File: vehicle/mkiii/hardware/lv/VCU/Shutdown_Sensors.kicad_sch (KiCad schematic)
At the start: 11 parts, among them Q5 SSM3K333R,LF, Q6 SSM3K333R,LF

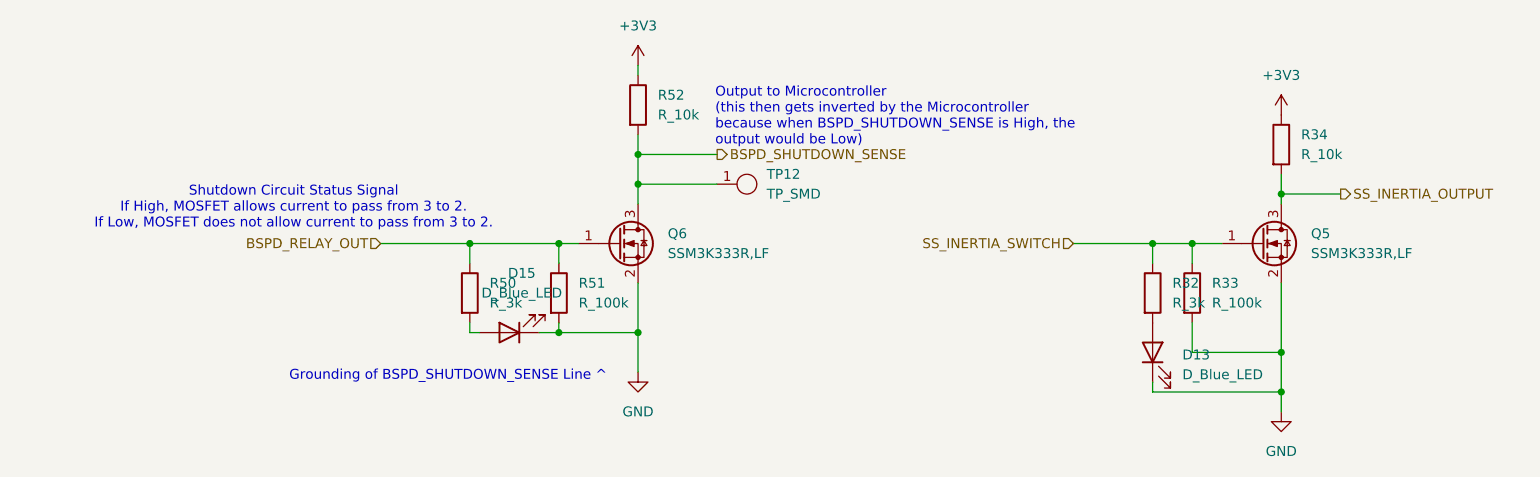
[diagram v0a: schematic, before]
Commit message: Layout completed, review required
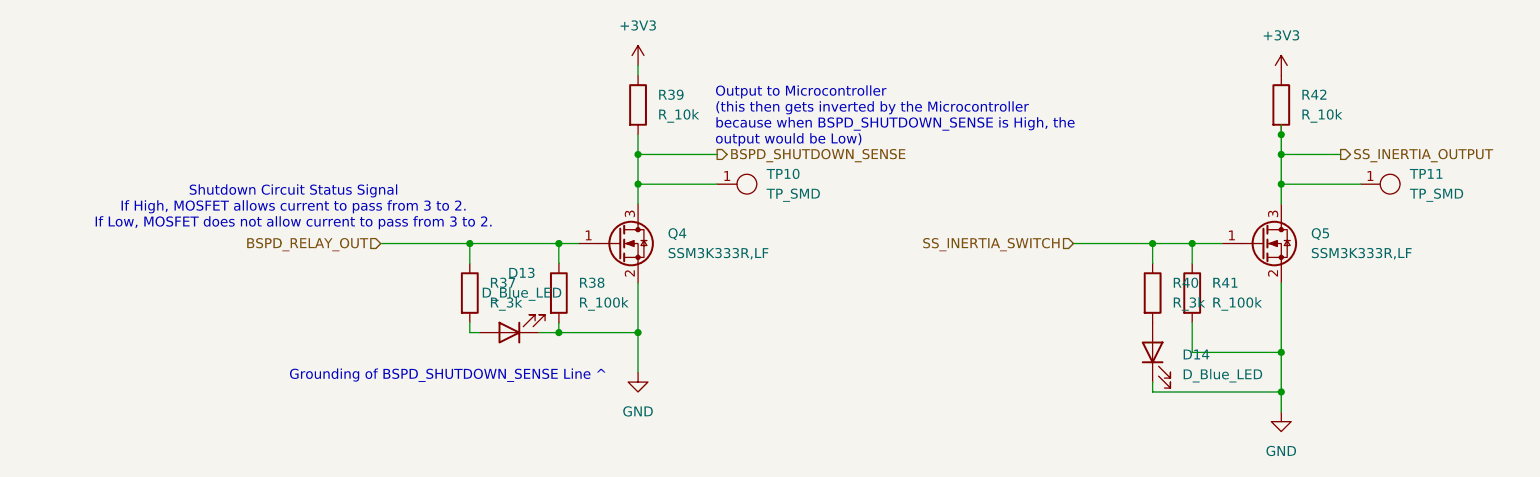
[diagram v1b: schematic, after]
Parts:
- added TP11: TP_SMD, OEM:TP_Hook_SMD, symbol OEM:TP_Hook_SMD
- renumbered D15 to D13, D13 to D14, Q6 to Q4, R50 to R37, R51 to R38, R52 to R39, R32 to R40, R33 to R41, R34 to R42, TP12 to TP10
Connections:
- net SS_INERTIA_OUTPUT: now also TP11.1
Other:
- moved on the sheet: R42
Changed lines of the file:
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@@
+	)
+	(junction
+		(at 201.93 83.82)
+		(diameter 0)
+		(color 0 0 0 0)
 	)
 	(junction
@@
 	)
 	(junction
+		(at 201.93 81.28)
+		(diameter 0)
+		(color 0 0 0 0)
+	)
+	(junction
 		(at 201.93 109.22)
 		(diameter 0)
@@
 	)
 	(junction
-		(at 201.93 88.9)
+		(at 201.93 87.63)
 		(diameter 0)
 		(color 0 0 0 0)
@@
 	(wire
 		(pts
+			(xy 201.93 87.63) (xy 201.93 90.17)
+		)
+		(stroke
+			(width 0)
+			(type default)
+		)
+	)
+	(wire
+		(pts
 			(xy 201.93 100.33) (xy 201.93 109.22)
 		)
@@
 	(wire
 		(pts
-			(xy 201.93 88.9) (xy 201.93 90.17)
-		)
-		(stroke
-			(width 0)
-			(type default)
-		)
-	)
-	(wire
-		(pts
 			(xy 86.36 95.25) (xy 97.79 95.25)
 		)
@@
 	(wire
 		(pts
-			(xy 201.93 86.36) (xy 201.93 88.9)
+			(xy 201.93 83.82) (xy 201.93 87.63)
+		)
+		(stroke
+			(width 0)
+			(type default)
+		)
+	)
+	(wire
+		(pts
+			(xy 201.93 81.28) (xy 201.93 83.82)
+		)
+		(stroke
+			(width 0)
+			(type default)
+		)
+	)
+	(wire
+		(pts
+			(xy 201.93 80.01) (xy 201.93 81.28)
 		)
 		(stroke
@@
 	(wire
 		(pts
-			(xy 201.93 88.9) (xy 209.55 88.9)
+			(xy 201.93 87.63) (xy 212.09 87.63)
+		)
+		(stroke
+			(width 0)
+			(type default)
+		)
+	)
+	(wire
+		(pts
+			(xy 201.93 83.82) (xy 209.55 83.82)
 		)
 		(stroke
@@
 	(hierarchical_label "SS_INERTIA_OUTPUT"
 		(shape output)
-		(at 209.55 88.9 0)
+		(at 209.55 83.82 0)
 		(effects
 			(font
@@
 	(symbol
 		(lib_id "OEM:R_10k_0.1W_0603")
-		(at 201.93 82.55 0)
+		(at 201.93 77.47 0)
 		(unit 1)
 		(exclude_from_sim no)
@@
 		(dnp no)
 		(fields_autoplaced yes)
-		(property "Reference" "R34"
-			(at 204.47 81.2799 0)
+		(property "Reference" "R42"
+			(at 204.47 76.1999 0)
 			(effects
 				(font
@@
 		)
 		(property "Value" "R_10k"
-			(at 204.47 83.8199 0)
+			(at 204.47 78.7399 0)
 			(effects
 				(font
@@
 		)
 		(property "Footprint" "OEM:R_0603_1608Metric"
-			(at 200.152 82.55 90)
+			(at 200.152 77.47 90)
 			(effects
 				(font
@@
 		)
 		(property "Datasheet" "https://www.mouser.com/datasheet/3/1099/1/SEI-RMCF_RMCP.pdf"
-			(at 201.93 82.55 0)
+			(at 201.93 77.47 0)
 			(effects
 				(font
@@
 		)
 		(property "Description" "RES 10K OHM 1% 1/10W 0603"
-			(at 201.93 82.55 0)
+			(at 201.93 77.47 0)
 			(effects
 				(font
@@
 		)
 		(property "MPN" "RMCF0603FT10K0"
-			(at 201.93 82.55 0)
+			(at 201.93 77.47 0)
 			(effects
 				(font
@@
 			(project "VCU"
 				(path "/ec5dd9e3-3092-4af4-bee1-94131d9ab7f8/f55c9820-8c9e-45b3-8461-692c1237659f"
-					(reference "R34")
+					(reference "R42")
 					(unit 1)
 				)
@@
 		(dnp no)
 		(fields_autoplaced yes)
-		(property "Reference" "R33"
+		(property "Reference" "R41"
 			(at 193.04 100.3299 0)
 			(effects
@@
 			(project "VCU"
 				(path "/ec5dd9e3-3092-4af4-bee1-94131d9ab7f8/f55c9820-8c9e-45b3-8461-692c1237659f"
-					(reference "R33")
+					(reference "R41")
+					(unit 1)
+				)
+			)
+		)
+	)
+	(symbol
+		(lib_id "OEM:TP_Hook_SMD")
+		(at 213.36 87.63 270)
+		(unit 1)
+		(exclude_from_sim no)
+		(in_bom yes)
+		(on_board yes)
+		(dnp no)
+		(fields_autoplaced yes)
+		(property "Reference" "TP11"
+			(at 218.44 86.3599 90)
+			(effects
+				(font
+					(size 1.27 1.27)
+				)
+				(justify left)
+			)
+		)
+		(property "Value" "TP_SMD"
+			(at 218.44 88.8999 90)
+			(effects
+				(font
+					(size 1.27 1.27)
+				)
+				(justify left)
+			)
+		)
+		(property "Footprint" "OEM:TP_Hook_SMD"
+			(at 209.55 87.63 0)
+			(effects
+				(font
+					(size 1.27 1.27)
+				)
+				(hide yes)
+			)
+		)
+		(property "Datasheet" "https://www.mouser.com/datasheet/3/201/1/5019.PDF"
+			(at 213.36 87.63 0)
+			(effects
+				(font
+					(size 1.27 1.27)
+				)
+				(hide yes)
+			)
+		)
+		(property "Description" "Test Point SMD Hook"
+			(at 213.36 87.63 0)
+			(effects
+				(font
+					(size 1.27 1.27)
+				)
+				(hide yes)
+			)
+		)
+		(property "MPN" "5019"
+			(at 213.36 87.63 0)
+			(effects
+				(font
+					(size 1.27 1.27)
+				)
+				(hide yes)
+			)
+		)
+		(pin "1"
+		)
+		(instances
+			(project "VCU"
+				(path "/ec5dd9e3-3092-4af4-bee1-94131d9ab7f8/f55c9820-8c9e-45b3-8461-692c1237659f"
+					(reference "TP11")
 					(unit 1)
 				)
@@
 		(dnp no)
 		(fields_autoplaced yes)
-		(property "Reference" "R52"
+		(property "Reference" "R39"
 			(at 121.92 76.1999 0)
 			(effects
@@
 			(project "VCU"
 				(path "/ec5dd9e3-3092-4af4-bee1-94131d9ab7f8/f55c9820-8c9e-45b3-8461-692c1237659f"
-					(reference "R52")
+					(reference "R39")
 					(unit 1)
 				)
@@
 		(dnp no)
 		(fields_autoplaced yes)
-		(property "Reference" "Q6"
+		(property "Reference" "Q4"
 			(at 123.19 93.9799 0)
 			(effects
@@
 			(project "VCU"
 				(path "/ec5dd9e3-3092-4af4-bee1-94131d9ab7f8/f55c9820-8c9e-45b3-8461-692c1237659f"
-					(reference "Q6")
+					(reference "Q4")
 					(unit 1)
 				)
@@
 		(dnp no)
 		(fields_autoplaced yes)
-		(property "Reference" "R51"
+		(property "Reference" "R38"
 			(at 111.76 100.3299 0)
 			(effects
@@
 			(project "VCU"
 				(path "/ec5dd9e3-3092-4af4-bee1-94131d9ab7f8/f55c9820-8c9e-45b3-8461-692c1237659f"
-					(reference "R51")
+					(reference "R38")
 					(unit 1)
 				)
@@
 		(dnp no)
 		(fields_autoplaced yes)
-		(property "Reference" "R32"
+		(property "Reference" "R40"
 			(at 187.96 100.3299 0)
 			(effects
@@
 			(project "VCU"
 				(path "/ec5dd9e3-3092-4af4-bee1-94131d9ab7f8/f55c9820-8c9e-45b3-8461-692c1237659f"
-					(reference "R32")
+					(reference "R40")
 					(unit 1)
 				)
@@
 		(dnp no)
 		(fields_autoplaced yes)
-		(property "Reference" "D13"
+		(property "Reference" "D14"
 			(at 189.23 109.5374 90)
 			(effects
@@
 			(project "VCU"
 				(path "/ec5dd9e3-3092-4af4-bee1-94131d9ab7f8/f55c9820-8c9e-45b3-8461-692c1237659f"
-					(reference "D13")
+					(reference "D14")
 					(unit 1)
 				)
@@
 		(dnp no)
 		(fields_autoplaced yes)
-		(property "Reference" "TP12"
+		(property "Reference" "TP10"
 			(at 135.89 86.3599 90)
 			(effects
@@
 			(project "VCU"
 				(path "/ec5dd9e3-3092-4af4-bee1-94131d9ab7f8/f55c9820-8c9e-45b3-8461-692c1237659f"
-					(reference "TP12")
+					(reference "TP10")
 					(unit 1)
 				)
@@
 	(symbol
 		(lib_id "power:+3V3")
-		(at 201.93 78.74 0)
+		(at 201.93 73.66 0)
 		(unit 1)
 		(exclude_from_sim no)
@@
 		(fields_autoplaced yes)
 		(property "Reference" "#PWR?"
-			(at 201.93 82.55 0)
+			(at 201.93 77.47 0)
 			(effects
 				(font
@@
 		)
 		(property "Value" "+3V3"
+			(at 201.93 68.58 0)
+			(effects
+				(font
+					(size 1.27 1.27)
+				)
+			)
+		)
+		(property "Footprint" ""
 			(at 201.93 73.66 0)
 			(effects
@@
 					(size 1.27 1.27)
 				)
-			)
-		)
-		(property "Footprint" ""
-			(at 201.93 78.74 0)
-			(effects
-				(font
-					(size 1.27 1.27)
-				)
 				(hide yes)
 			)
 		)
 		(property "Datasheet" ""
-			(at 201.93 78.74 0)
+			(at 201.93 73.66 0)
 			(effects
 				(font
@@
 		)
 		(property "Description" "Power symbol creates a global label with name \"+3V3\""
-			(at 201.93 78.74 0)
+			(at 201.93 73.66 0)
 			(effects
 				(font
@@
 		(dnp no)
 		(fields_autoplaced yes)
-		(property "Reference" "D15"
+		(property "Reference" "D13"
 			(at 104.4575 99.06 0)
 			(effects
@@
 			(project "VCU"
 				(path "/ec5dd9e3-3092-4af4-bee1-94131d9ab7f8/f55c9820-8c9e-45b3-8461-692c1237659f"
-					(reference "D15")
+					(reference "D13")
 					(unit 1)
 				)
@@
 		(dnp no)
 		(fields_autoplaced yes)
-		(property "Reference" "R50"
+		(property "Reference" "R37"
 			(at 100.33 100.3299 0)
 			(effects
@@
 			(project "VCU"
 				(path "/ec5dd9e3-3092-4af4-bee1-94131d9ab7f8/f55c9820-8c9e-45b3-8461-692c1237659f"
-					(reference "R50")
+					(reference "R37")
 					(unit 1)
 				)

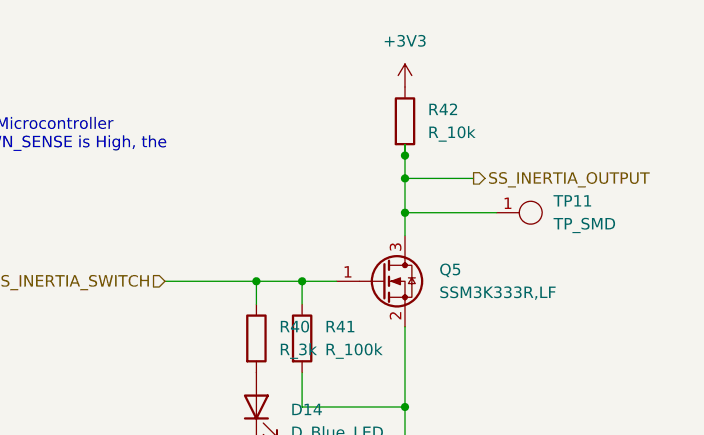
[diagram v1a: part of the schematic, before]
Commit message: Minor ERC Fixes in Schematics; Minor Silkscreen Changes; Addedc Subteam Layout; Added Production Files.
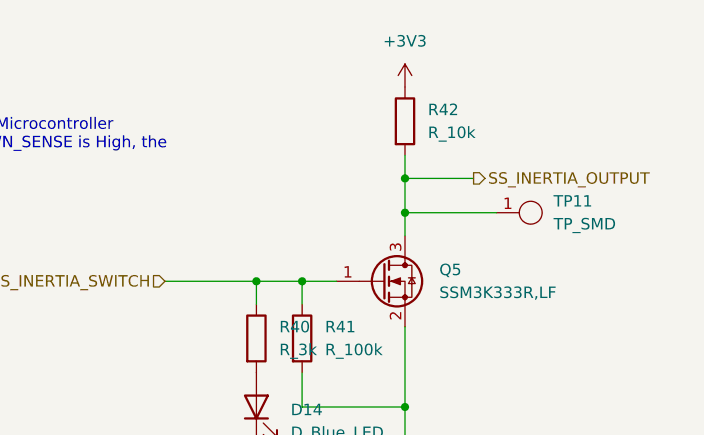
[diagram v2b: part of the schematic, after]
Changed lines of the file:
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@@
-	)
-	(junction
-		(at 201.93 81.28)
-		(diameter 0)
-		(color 0 0 0 0)
 	)
 	(junction
@@
 		(pts
 			(xy 201.93 81.28) (xy 201.93 83.82)
-		)
-		(stroke
-			(width 0)
-			(type default)
-		)
-	)
-	(wire
-		(pts
-			(xy 201.93 80.01) (xy 201.93 81.28)
 		)
 		(stroke
@@
 		(dnp no)
 		(fields_autoplaced yes)
-		(property "Reference" "#PWR?"
+		(property "Reference" "#PWR0195"
 			(at 119.38 118.11 0)
 			(effects
@@
 			(project "VCU"
 				(path "/ec5dd9e3-3092-4af4-bee1-94131d9ab7f8/f55c9820-8c9e-45b3-8461-692c1237659f"
-					(reference "#PWR?")
+					(reference "#PWR0195")
 					(unit 1)
 				)
@@
 		(dnp no)
 		(fields_autoplaced yes)
-		(property "Reference" "#PWR?"
+		(property "Reference" "#PWR0196"
 			(at 119.38 76.2 0)
 			(effects
@@
 			(project "VCU"
 				(path "/ec5dd9e3-3092-4af4-bee1-94131d9ab7f8/f55c9820-8c9e-45b3-8461-692c1237659f"
-					(reference "#PWR?")
+					(reference "#PWR0196")
 					(unit 1)
 				)
@@
 		(dnp no)
 		(fields_autoplaced yes)
-		(property "Reference" "#PWR?"
+		(property "Reference" "#PWR0197"
 			(at 201.93 77.47 0)
 			(effects
@@
 			(project "VCU"
 				(path "/ec5dd9e3-3092-4af4-bee1-94131d9ab7f8/f55c9820-8c9e-45b3-8461-692c1237659f"
-					(reference "#PWR?")
+					(reference "#PWR0197")
 					(unit 1)
 				)
@@
 		(dnp no)
 		(fields_autoplaced yes)
-		(property "Reference" "#PWR?"
+		(property "Reference" "#PWR0198"
 			(at 201.93 123.19 0)
 			(effects
@@
 			(project "VCU"
 				(path "/ec5dd9e3-3092-4af4-bee1-94131d9ab7f8/f55c9820-8c9e-45b3-8461-692c1237659f"
-					(reference "#PWR?")
+					(reference "#PWR0198")
 					(unit 1)
 				)
